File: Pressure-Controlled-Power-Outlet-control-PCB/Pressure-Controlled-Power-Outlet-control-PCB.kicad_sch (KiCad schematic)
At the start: 4 parts, among them J1 SEN0257 Connector, U1 Pico

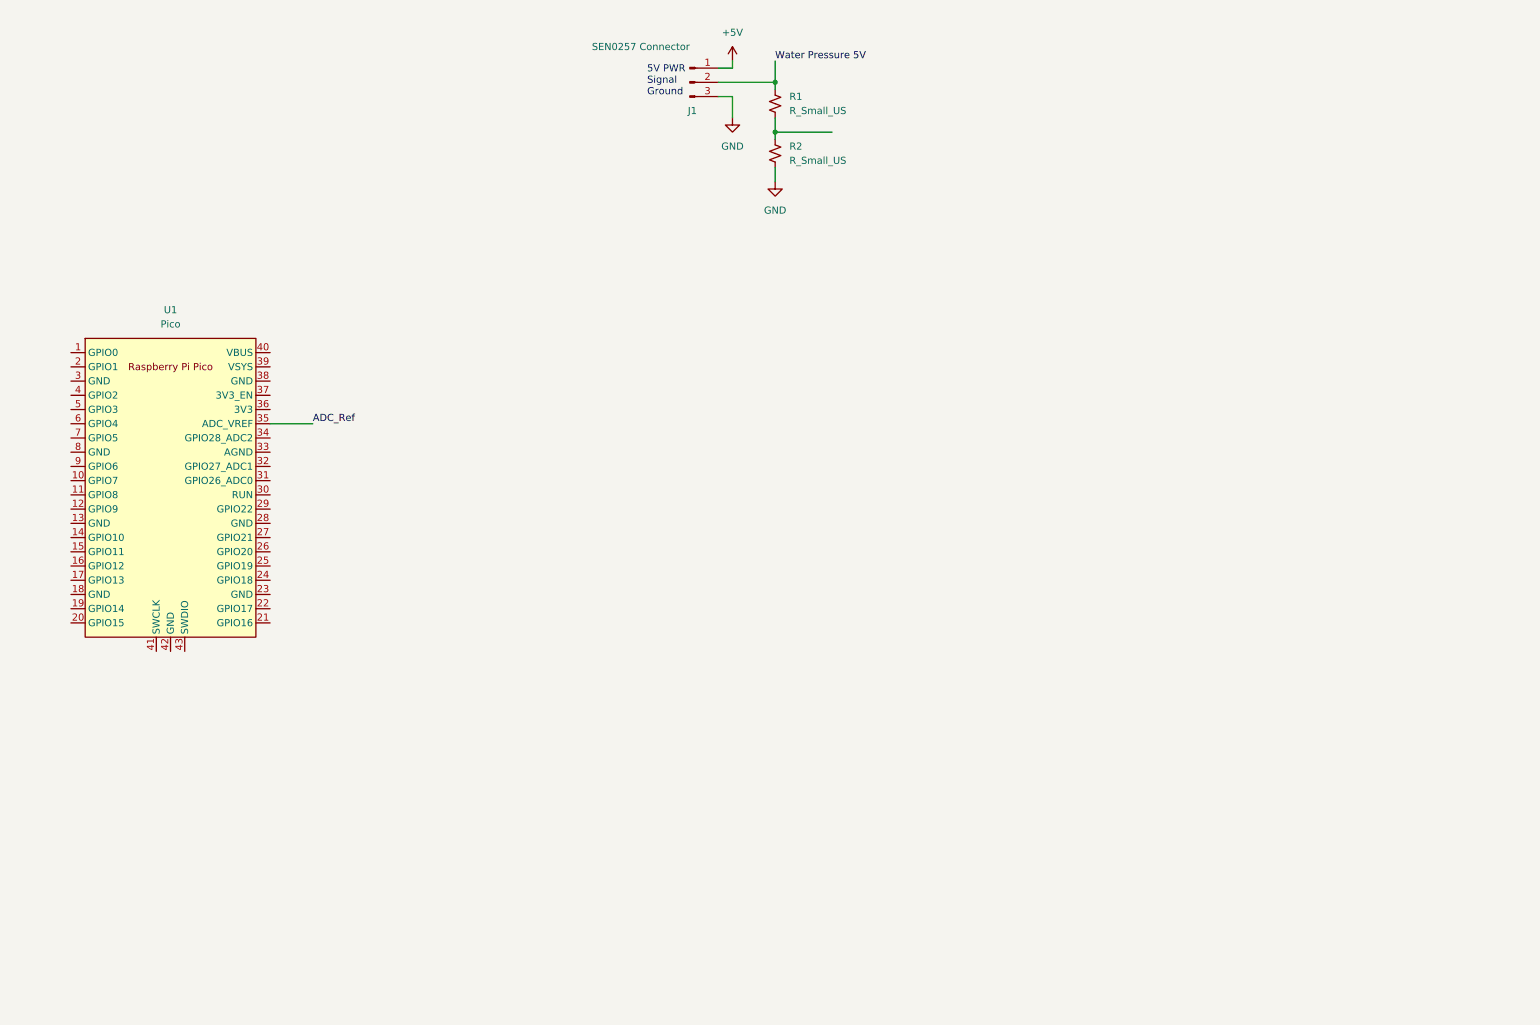
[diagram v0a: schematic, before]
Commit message: created a 5v logic to 3.3v logic for the water sensor
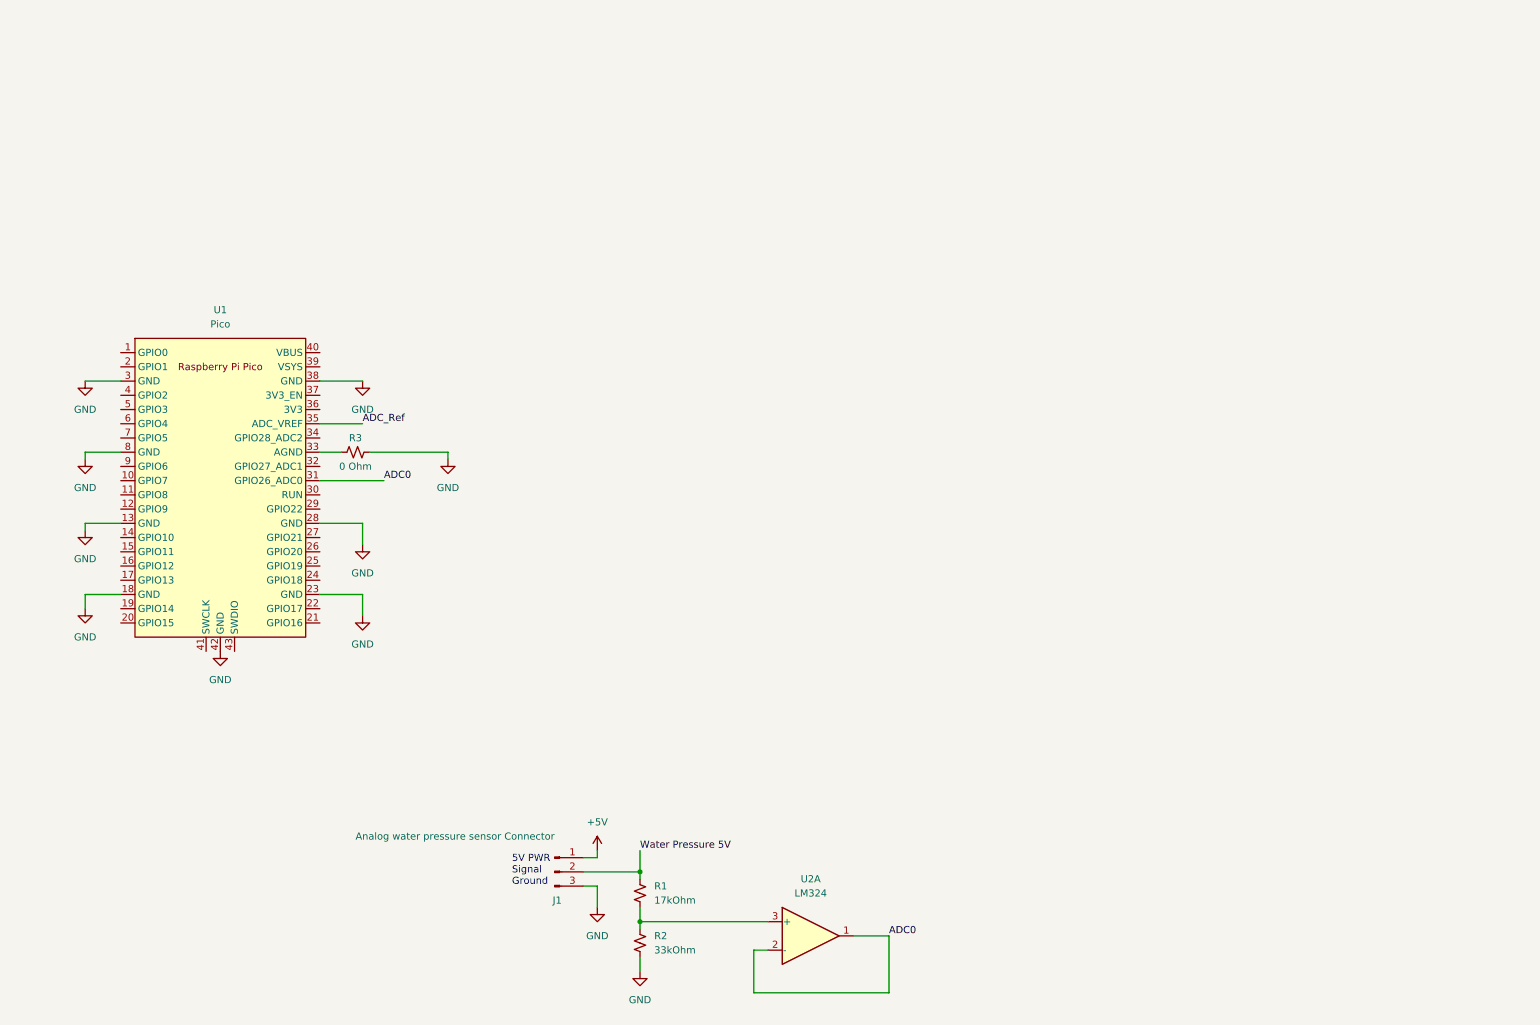
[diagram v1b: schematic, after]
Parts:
- added R3: 0 Ohm, symbol Device:R_Small_US
- added U2: LM324, symbol Amplifier_Operational:LM324
- J1: value SEN0257 Connector -> Analog water pressure sensor Connector
- R1: value R_Small_US -> 17kOhm
- R2: value R_Small_US -> 33kOhm
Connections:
- net GND: now also U1.13 (GND), U1.18 (GND), U1.23 (GND), U1.28 (GND), U1.3 (GND), U1.38 (GND), U1.42 (GND), U1.8 (GND), R3.2
- net at R1.2, R2.1: now also U2.3 (+)
- net ADC0: now reaches U1.31 (GPIO26_ADC0)
- net ADC0: now also U2.1, U2.2 (-)
- net at U1.33 (AGND): now also R3.1
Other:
- moved on the sheet: J1, R1, R2, U1

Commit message: have most of the traces ran on pcb but controlling the relays
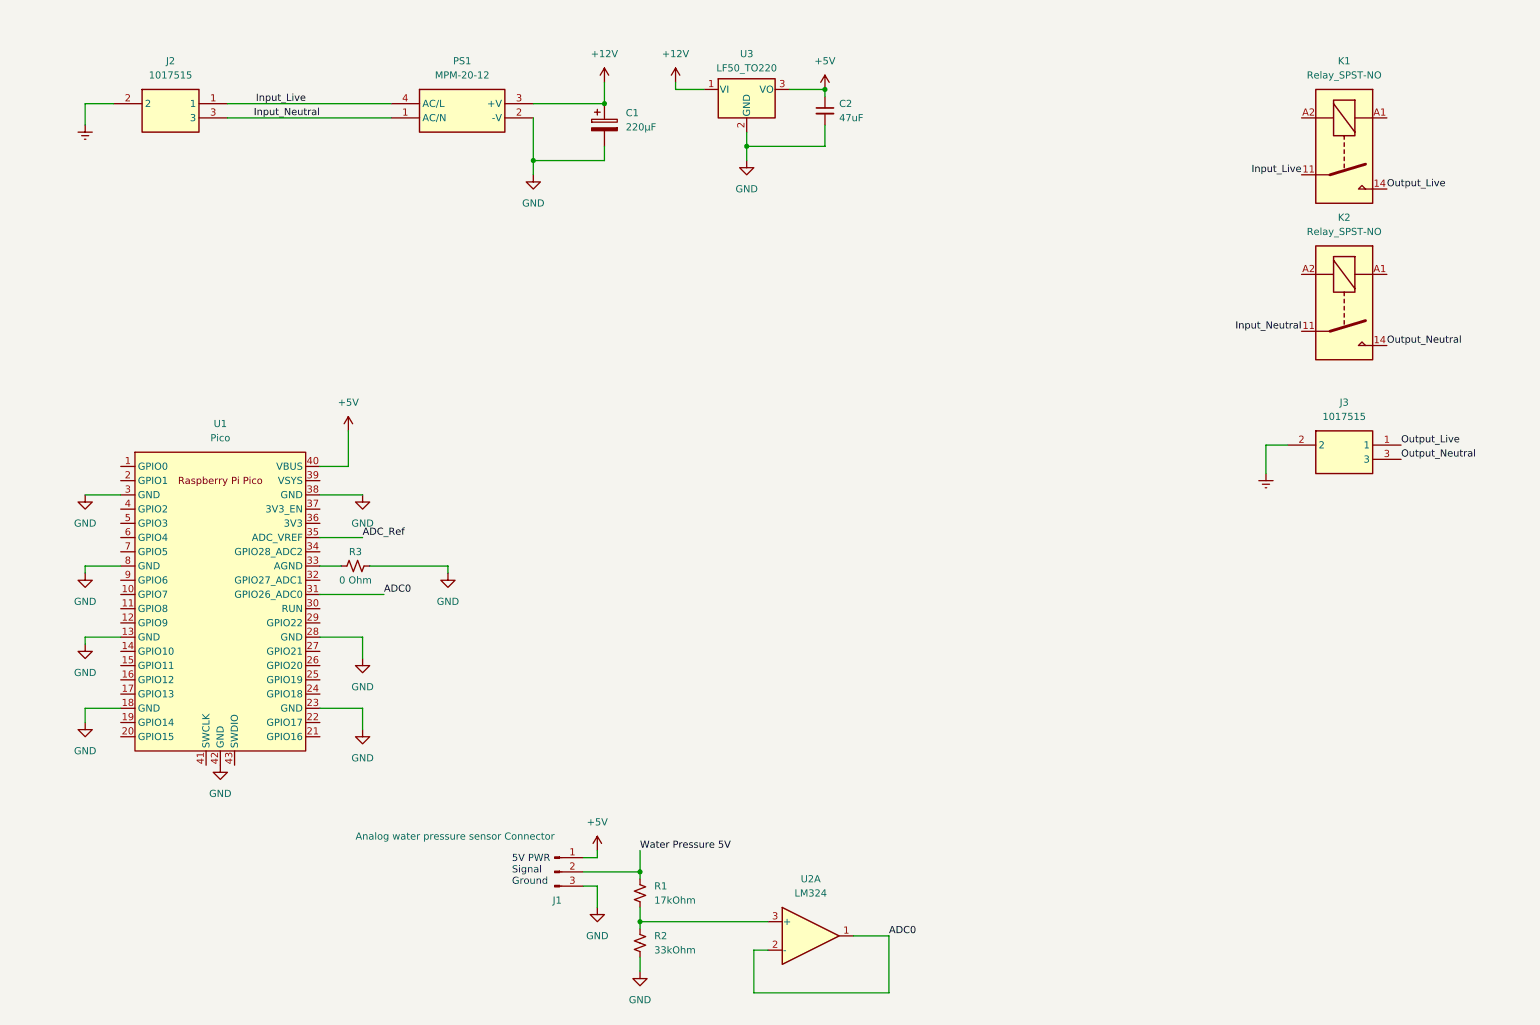
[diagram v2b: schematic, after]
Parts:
- added C1: 220µF, Capacitor_THT:CP_Radial_Tantal_D6.0mm_P2.50mm, symbol Device:C_Polarized
- added C2: 47uF, Capacitor_THT:CP_Radial_D6.3mm_P2.50mm, symbol Device:C_Small
- added J2, J3: 1017515, Extra:1017515, symbol Extra:1017515
- added K1, K2: Relay_SPST-NO, Relay_THT:Relay_1-Form-A_Schrack-RYII_RM5mm, symbol Relay:Relay_SPST-NO
- added PS1: MPM-20-12, Extra:MPM2012, symbol Extra:MPM-20-12
- added U3: LF50_TO220, Package_TO_SOT_THT:TO-220-3_Vertical, symbol Regulator_Linear:LF50_TO220
- J1: footprint (none) -> Connector_PinSocket_2.54mm:PinSocket_1x03_P2.54mm_Vertical
- R1, R2: footprint (none) -> Resistor_THT:R_Axial_DIN0414_L11.9mm_D4.5mm_P5.08mm_Vertical
- R3: footprint (none) -> Resistor_THT:R_Axial_DIN0207_L6.3mm_D2.5mm_P2.54mm_Vertical
- U2: footprint (none) -> Package_DIP:DIP-14_W7.62mm_LongPads
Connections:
- net +5V: now also U1.40 (VBUS), C2.1, U3.3 (VO)
- net GND: now also C1.2, C2.2, PS1.2 (-V), U3.2 (GND)
- new net +12V: C1.1, PS1.3 (+V), U3.1 (VI)
- new net Earth: J2.2, J3.2
- new net Input_Live: J2.1, K1.11, PS1.4 (AC/L)
- new net Input_Neutral: J2.3, K2.11, PS1.1 (AC/N)
- new net Output_Live: J3.1, K1.14
- new net Output_Neutral: J3.3, K2.14
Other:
- moved on the sheet: R3, U1

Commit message: removed onboard power supply and replaced it with an external 24V PSU, and removed High voltage pcb connections as relays have connectors on the top of them
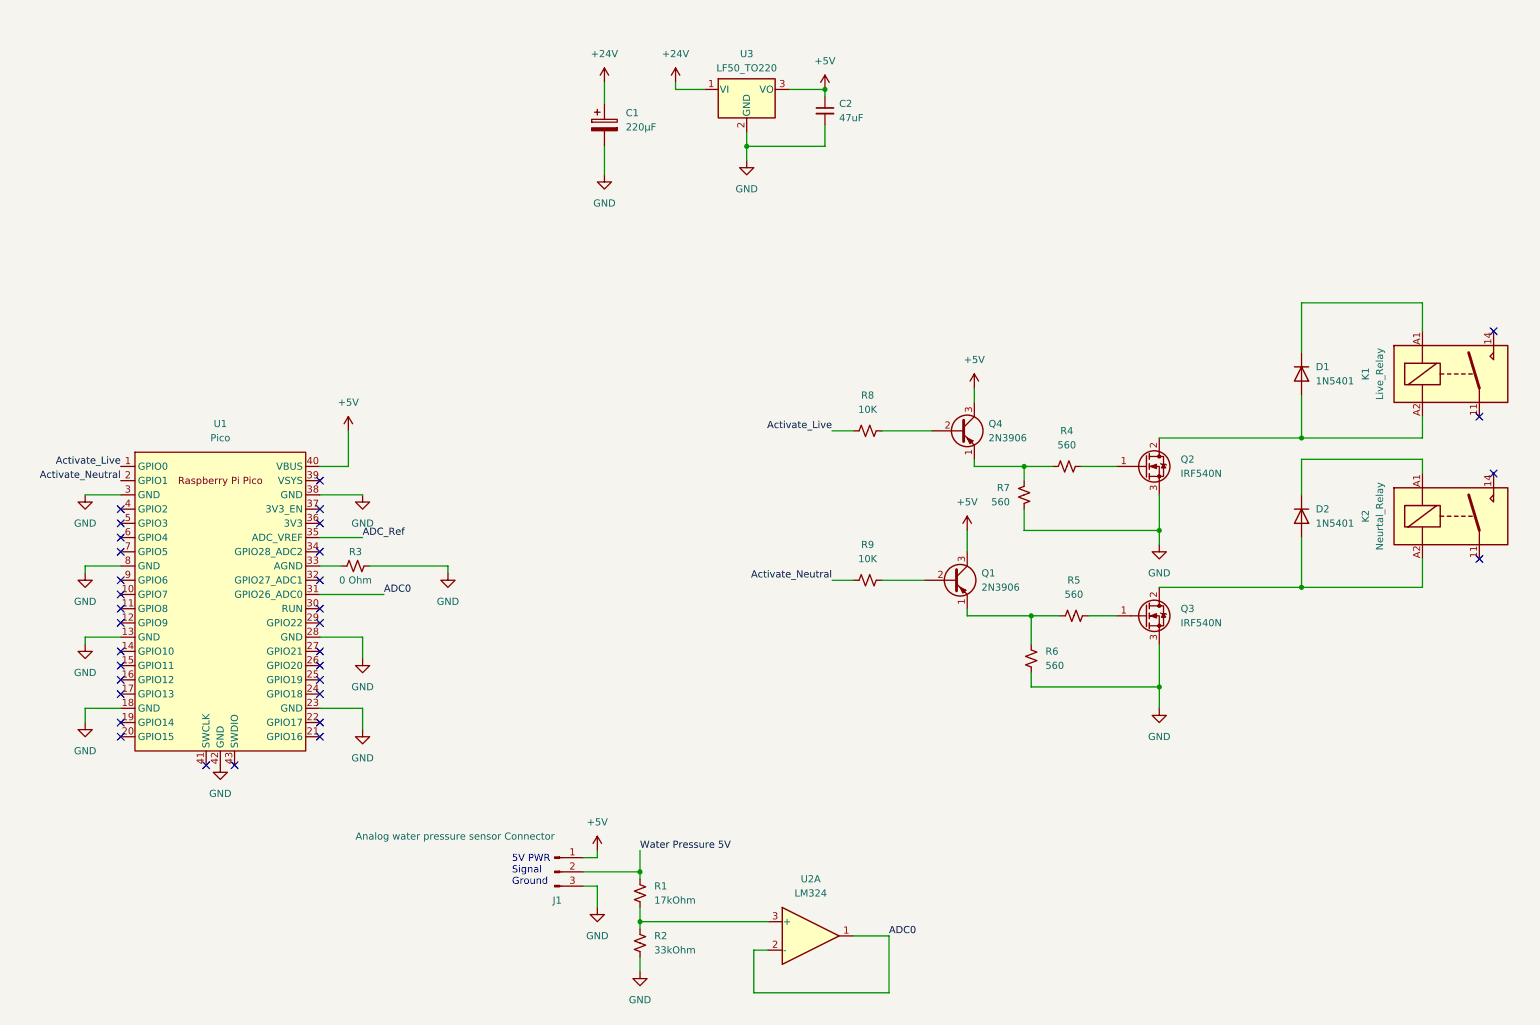
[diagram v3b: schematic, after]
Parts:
- removed J2, J3: 1017515, Extra:1017515, symbol Extra:1017515
- removed PS1: MPM-20-12, Extra:MPM2012, symbol Extra:MPM-20-12
- added D1, D2: 1N5401, Diode_THT:D_DO-201AD_P15.24mm_Horizontal, symbol Diode:1N5401
- added Q1, Q4: 2N3906, Package_TO_SOT_THT:TO-92_Inline, symbol Transistor_BJT:2N3906
- added Q2, Q3: IRF540N, Package_TO_SOT_THT:TO-220-3_Vertical, symbol Transistor_FET:IRF540N
- added R4, R5, R6, R7: 560, Resistor_THT:R_Axial_DIN0207_L6.3mm_D2.5mm_P2.54mm_Vertical, symbol Device:R_Small_US
- added R8, R9: 10K, Resistor_THT:R_Axial_DIN0207_L6.3mm_D2.5mm_P2.54mm_Vertical, symbol Device:R_Small_US
- K1: value Relay_SPST-NO -> Live_Relay
- K2: value Relay_SPST-NO -> Neurtal_Relay
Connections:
- net +5V: now also Q1.3 (C), Q4.3 (C)
- net GND: now also Q2.3 (S), Q3.3 (S), R6.1, R7.1
- net Activate_Live: now reaches U1.1 (GPIO0)
- net Activate_Live: now also R8.1
- net Activate_Neutral: now reaches U1.2 (GPIO1)
- net Activate_Neutral: now also R9.1
- net at K1.A1: now also D1.1 (K)
- net at K1.A2: now also D1.2 (A), Q2.2 (D)
- net at K2.A1: now also D2.1 (K)
- net at K2.A2: now also D2.2 (A), Q3.2 (D)
- net +12V renamed +24V
- net Input_Live: no longer names the net of K1.11
- net Input_Neutral: no longer names the net of K2.11
- net Output_Live: no longer names the net of K1.14
- net Output_Neutral: no longer names the net of K2.14
- new net: Q4.2 (B), R8.2
- new net: Q3.1 (G), R5.2
- new net: Q1.1 (E), R5.1, R6.2
- new net: Q1.2 (B), R9.2
- new net: Q2.1 (G), R4.2
- new net: Q4.1 (E), R4.1, R7.2
- no-connect marks 0 -> 33
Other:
- moved on the sheet: K1, K2

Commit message: wired PCB but the footprint does not match the relay im using so i need to swap the relay :(
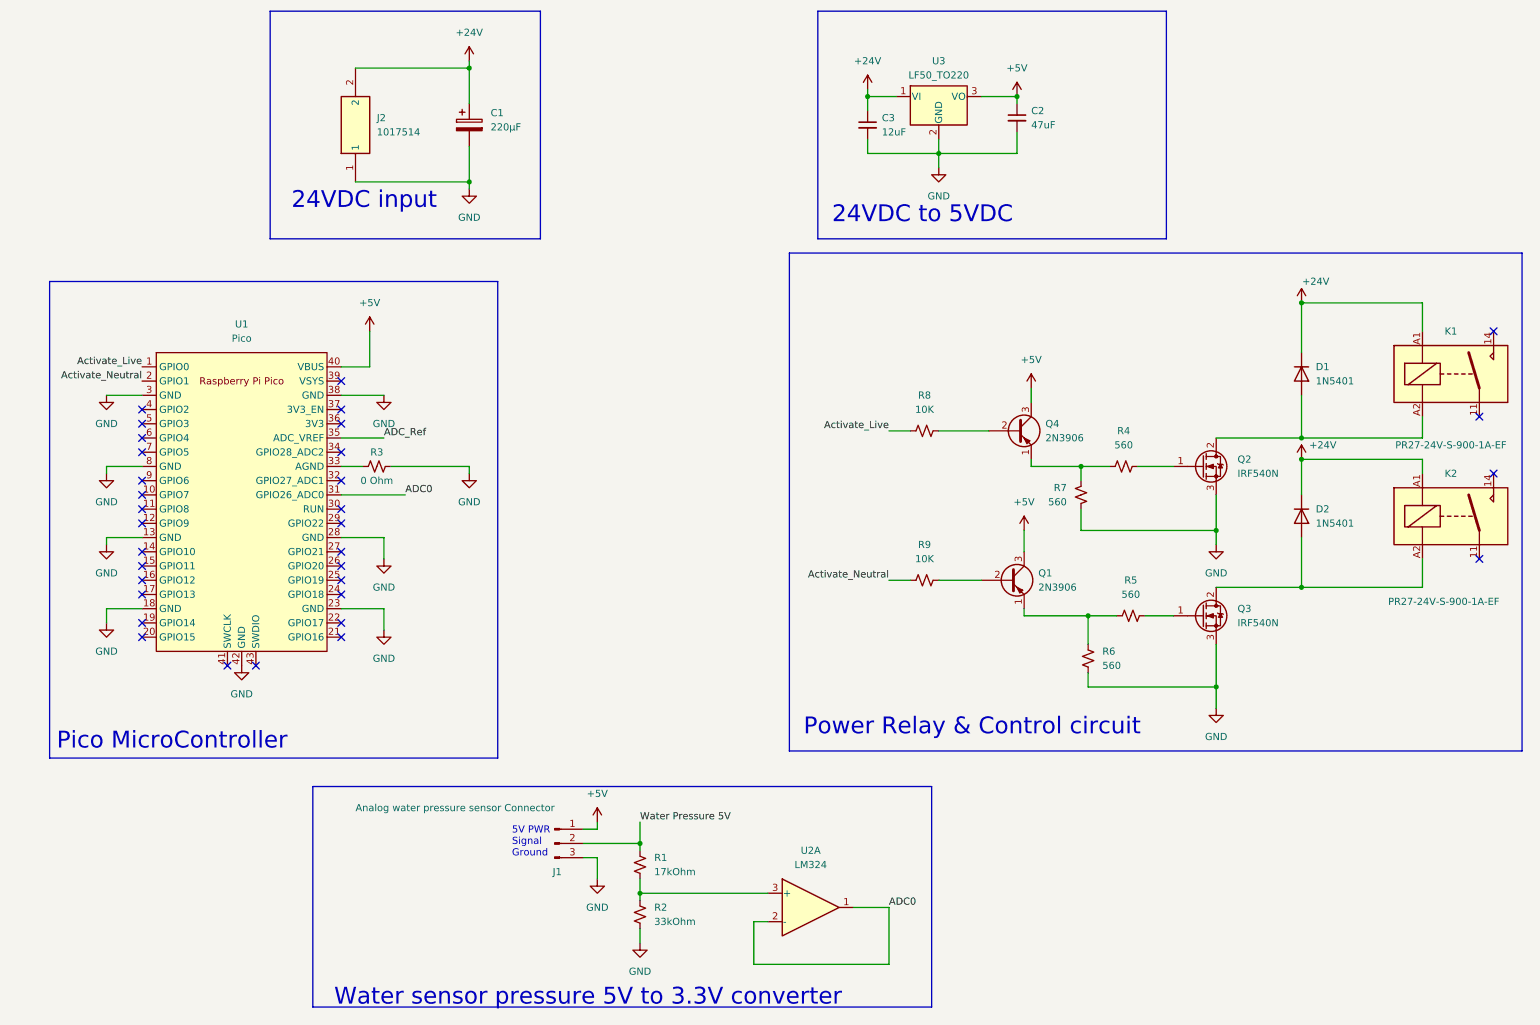
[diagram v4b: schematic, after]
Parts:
- added C3: 12uF, Capacitor_THT:CP_Radial_D4.0mm_P2.00mm, symbol Device:C_Small
- added J2: 1017514, Extra:1017514, symbol Extra:1017514
- K1: value Live_Relay -> PR27-24V-S-900-1A-EF
- K2: value Neurtal_Relay -> PR27-24V-S-900-1A-EF
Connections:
- net +24V: now also D1.1 (K), D2.1 (K), K1.A1, K2.A1, C3.1, J2.2
- net GND: now also C3.2, J2.1
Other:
- note added: "24VDC input"
- note added: "24VDC to 5VDC"
- note added: "Pico MicroController"
- note added: "Power Relay & Control circuit"
- note added: "Water sensor pressure 5V to 3.3V converter"
- moved on the sheet: C1, C2, J1, Q1, Q2, Q3, Q4, R1, R2, R3, R4, R5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
